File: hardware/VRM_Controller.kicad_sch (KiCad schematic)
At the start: 33 parts, among them J2001 Conn_01x02_Pin, J2002 Conn_01x02_Pin, J2003 Conn_01x02_Pin, J2004 Conn_01x02_Pin, U2001 TPS536C7B1RSLT

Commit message: feat(PCB): Vrms for mem and core layed out
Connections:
- net BVR_RDY is gone; now on net BRV_READY: R2014.2
- net at C2005.2, U2001.26 (AVSN): now also J2002.1 (Pin_1)
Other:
- note added: "Disconnecting the BVR_EN resistor will allow it to be configured by the micro controller as a Reset pin. The AVR_EN pin will controll both."
- note removed: "Add Reset Pin?"
- moved on the sheet: C2010, C2011, C2012, R2019, R2020

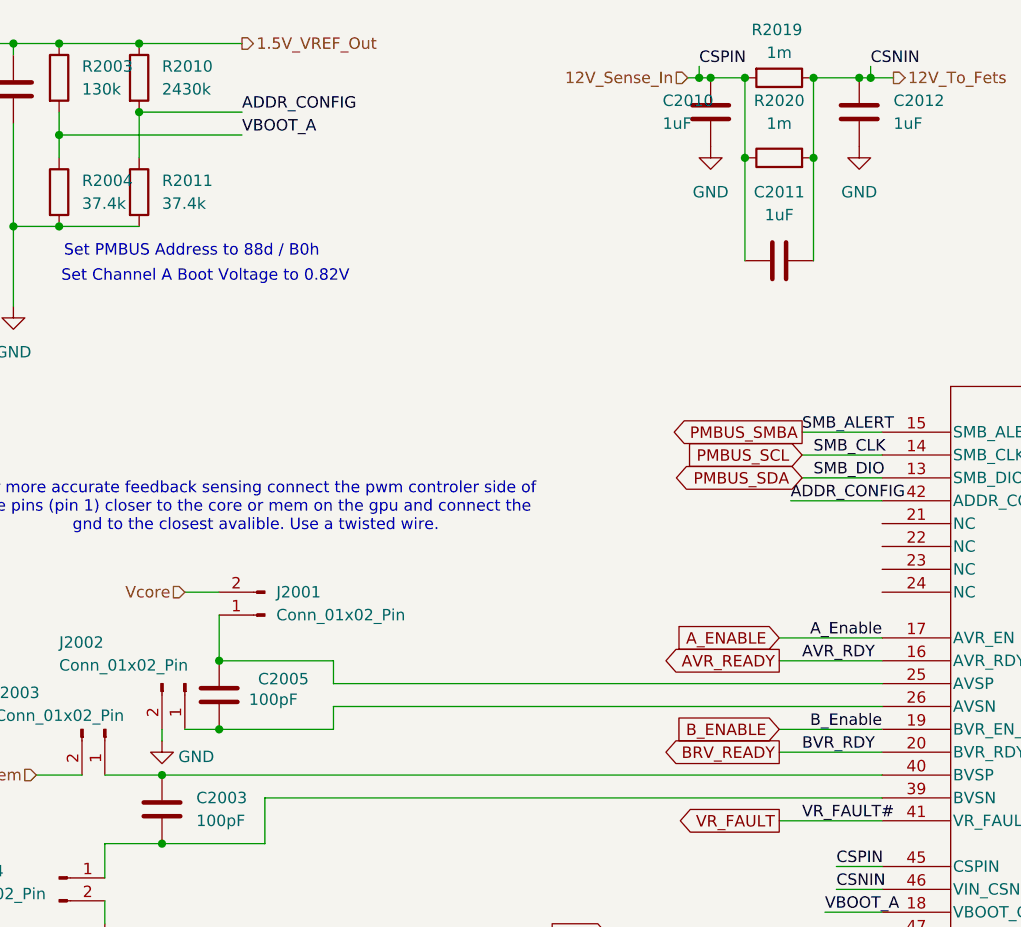
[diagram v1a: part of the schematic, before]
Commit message: feat(PCB): fix all DRC errors
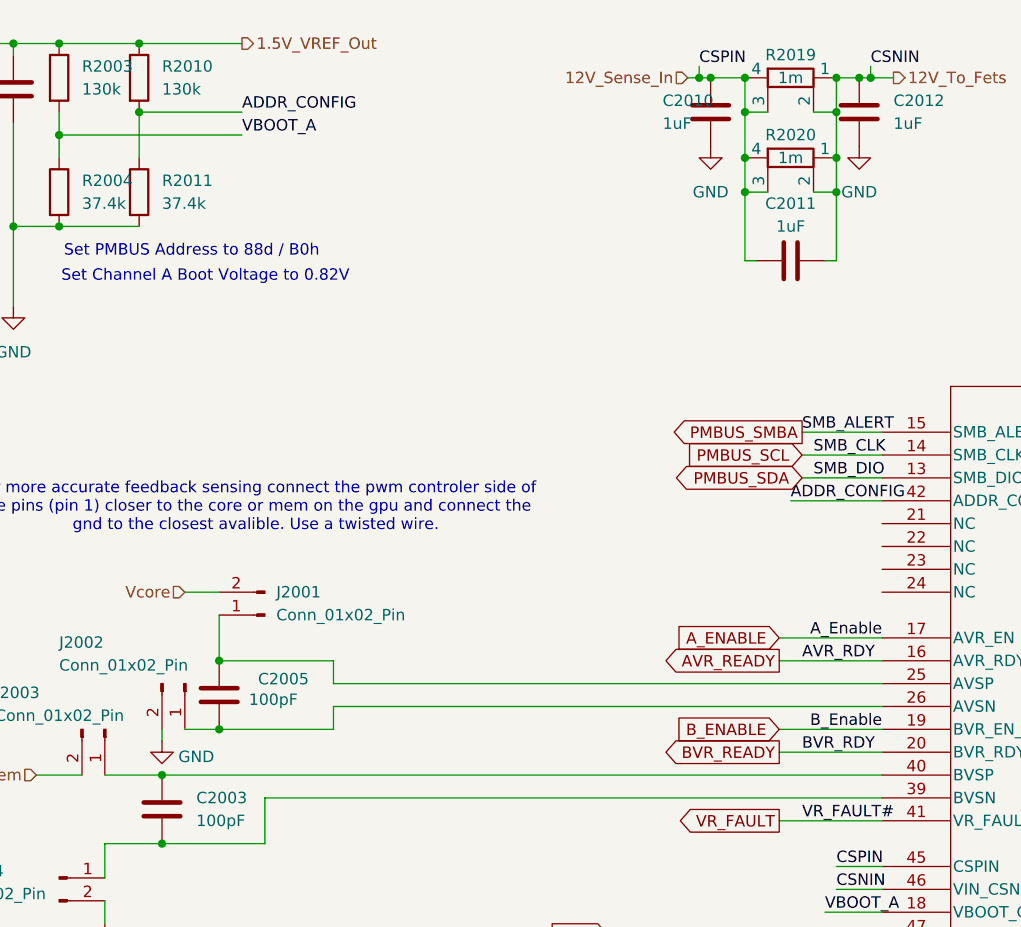
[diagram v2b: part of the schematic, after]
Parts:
- removed R2019: 1m, Resistor_SMD:R_Shunt_Vishay_WSK2512_6332Metric_T1.19mm, symbol Device:R
- added R2019: 1m, Resistor_SMD:R_Shunt_Vishay_WSK2512_6332Metric_T1.19mm, symbol Device:R_Shunt
- R2010: value 2430k -> 130k
- R2020: symbol Device:R -> Device:R_Shunt
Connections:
- net 12V_Sense_In: now also R2020.3, R2020.4, R2019.3, R2019.4; no longer R2020.1
- net 12V_To_Fets: now also R2020.1, R2019.1, R2019.2
- net BRV_READY renamed BVR_READY
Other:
- moved on the sheet: C2011

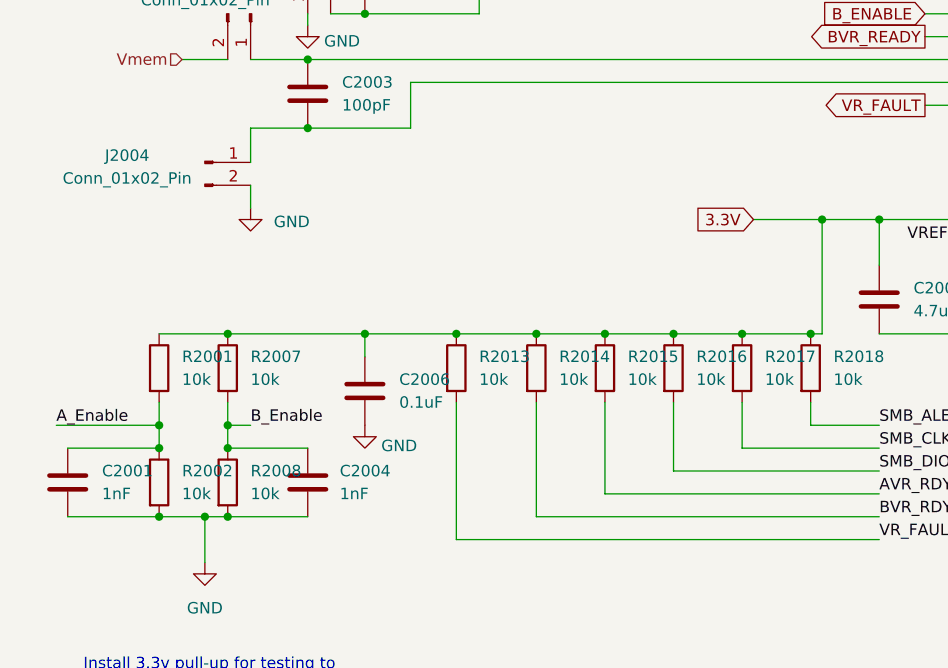
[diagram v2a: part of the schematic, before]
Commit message: feat(schematic): refactor main heirarchy
This commit makes a bunch of changes to how power is delivered on the
schematic. It also adds the probit header and the i2c output connector
on the main page of the schematic. Lastly, it changes it so that USB
power should work and also not power the 5V rail to the mosfet ICs.
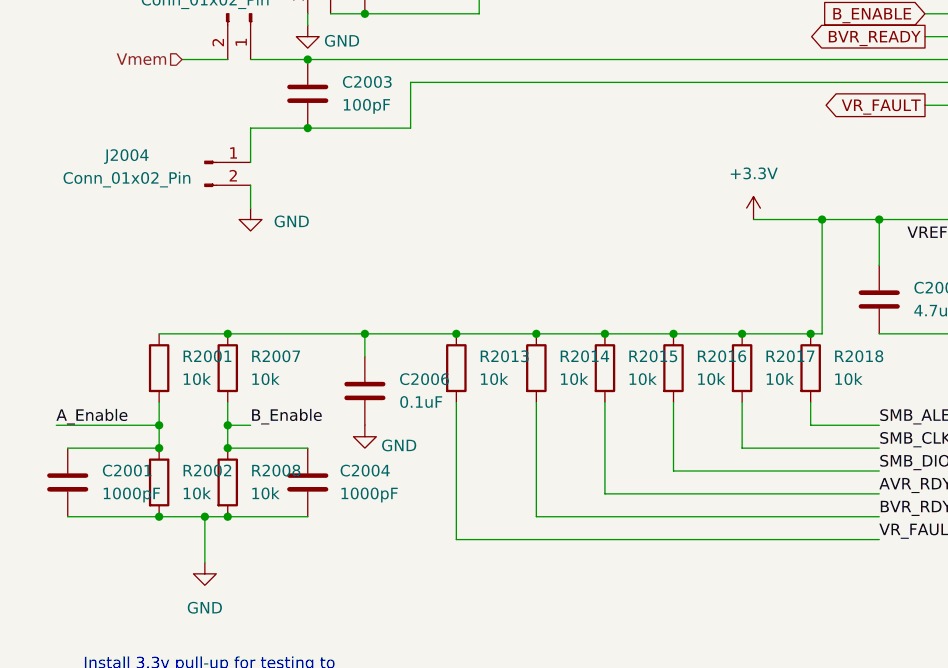
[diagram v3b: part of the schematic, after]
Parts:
- C2001, C2004: value 1nF -> 1000pF
- J2001, J2002, J2003, J2004: footprint Connector_PinHeader_2.54mm:PinHeader_1x02_P2.54mm_Vertical -> Connector_PinHeader_2.54mm:PinHeader_1x02_P2.54mm_Vertical_SMD_Pin1Right
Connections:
- net 3.3V renamed +3.3V
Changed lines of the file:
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@@
 	(label "CSPIN"
 		(at 101.6 20.32 0)
-		(fields_autoplaced yes)
 		(effects
 			(font
@@
 	(label "CSPIN"
 		(at 116.84 109.22 0)
-		(fields_autoplaced yes)
 		(effects
 			(font
@@
 	(label "VBOOT_A"
 		(at 115.57 114.3 0)
-		(fields_autoplaced yes)
 		(effects
 			(font
@@
 	(label "VR_FAULT#"
 		(at 113.03 104.14 0)
-		(fields_autoplaced yes)
 		(effects
 			(font
@@
 	(label "ADDR_CONFIG"
 		(at 111.76 68.58 0)
-		(fields_autoplaced yes)
 		(effects
 			(font
@@
 	(label "B_Enable"
 		(at 35.56 139.7 0)
-		(fields_autoplaced yes)
 		(effects
 			(font
@@
 	(label "VBOOT_A"
 		(at 50.8 27.94 0)
-		(fields_autoplaced yes)
 		(effects
 			(font
@@
 	(label "B_Enable"
 		(at 121.92 93.98 180)
-		(fields_autoplaced yes)
 		(effects
 			(font
@@
 	(label "AVR_RDY"
 		(at 113.03 86.36 0)
-		(fields_autoplaced yes)
 		(effects
 			(font
@@
 	(label "VREF"
 		(at 113.03 119.38 180)
-		(fields_autoplaced yes)
 		(effects
 			(font
@@
 	(label "CSNIN"
 		(at 120.65 20.32 0)
-		(fields_autoplaced yes)
 		(effects
 			(font
@@
 	(label "VREF"
 		(at 21.59 17.78 180)
-		(fields_autoplaced yes)
 		(effects
 			(font
@@
 	(label "CSNIN"
 		(at 116.84 111.76 0)
-		(fields_autoplaced yes)
 		(effects
 			(font
@@
 	(label "ADDR_CONFIG"
 		(at 50.8 25.4 0)
-		(fields_autoplaced yes)
 		(effects
 			(font
@@
 	(label "SMB_CLK"
 		(at 105.41 142.24 0)
-		(fields_autoplaced yes)
 		(effects
 			(font
@@
 	(label "SMB_ALERT"
 		(at 105.41 139.7 0)
-		(fields_autoplaced yes)
 		(effects
 			(font
@@
 	(label "SMB_CLK"
 		(at 114.3 63.5 0)
-		(fields_autoplaced yes)
 		(effects
 			(font
@@
 	(label "AVR_RDY"
 		(at 105.41 147.32 0)
-		(fields_autoplaced yes)
 		(effects
 			(font
@@
 	(label "BVR_RDY"
 		(at 113.03 96.52 0)
-		(fields_autoplaced yes)
 		(effects
 			(font
@@
 	(label "SMB_ALERT"
 		(at 113.03 60.96 0)
-		(fields_autoplaced yes)
 		(effects
 			(font
@@
 	(label "VR_FAULT#"
 		(at 105.41 152.4 0)
-		(fields_autoplaced yes)
 		(effects
 			(font
@@
 	(label "BVR_RDY"
 		(at 105.41 149.86 0)
-		(fields_autoplaced yes)
 		(effects
 			(font
@@
 	(label "A_Enable"
 		(at 121.92 83.82 180)
-		(fields_autoplaced yes)
 		(effects
 			(font
@@
 	(label "SMB_DIO"
 		(at 114.3 66.04 0)
-		(fields_autoplaced yes)
 		(effects
 			(font
@@
 	(label "SMB_DIO"
 		(at 105.41 144.78 0)
-		(fields_autoplaced yes)
 		(effects
 			(font
@@
 	(label "A_Enable"
 		(at 13.97 139.7 0)
-		(fields_autoplaced yes)
 		(effects
 			(font
@@
 		)
 	)
-	(global_label "3.3V"
-		(shape input)
-		(at 91.44 116.84 180)
-		(fields_autoplaced yes)
-		(effects
-			(font
-				(size 1.27 1.27)
-			)
-			(justify right)
-		)
-		(property "Intersheetrefs" "${INTERSHEET_REFS}"
-			(at 84.3424 116.84 0)
-			(effects
-				(font
-					(size 1.27 1.27)
-				)
-				(justify right)
-				(hide yes)
-			)
-		)
-	)
 	(hierarchical_label "Vmem"
 		(shape input)
 		(at 27.94 99.06 180)
-		(fields_autoplaced yes)
 		(effects
 			(font
@@
 		(shape input)
 		(at 100.33 21.59 180)
-		(fields_autoplaced yes)
 		(effects
 			(font
@@
 		(shape input)
 		(at 177.8 86.36 0)
-		(fields_autoplaced yes)
 		(effects
 			(font
@@
 		(shape input)
 		(at 177.8 81.28 0)
-		(fields_autoplaced yes)
 		(effects
 			(font
@@
 		(shape input)
 		(at 179.07 129.54 0)
-		(fields_autoplaced yes)
 		(effects
 			(font
@@
 		(shape output)
 		(at 177.8 68.58 0)
-		(fields_autoplaced yes)
 		(effects
 			(font
@@
 		(shape input)
 		(at 177.8 119.38 0)
-		(fields_autoplaced yes)
 		(effects
 			(font
@@
 		(shape input)
 		(at 177.8 91.44 0)
-		(fields_autoplaced yes)
 		(effects
 			(font
@@
 		(shape input)
 		(at 177.8 114.3 0)
-		(fields_autoplaced yes)
 		(effects
 			(font
@@
 		(shape output)
 		(at 177.8 99.06 0)
-		(fields_autoplaced yes)
 		(effects
 			(font
@@
 		(shape input)
 		(at 177.8 101.6 0)
-		(fields_autoplaced yes)
 		(effects
 			(font
@@
 		(shape output)
 		(at 177.8 93.98 0)
-		(fields_autoplaced yes)
 		(effects
 			(font
@@
 		(shape output)
 		(at 123.19 21.59 0)
-		(fields_autoplaced yes)
 		(effects
 			(font
@@
 		(shape output)
 		(at 177.8 104.14 0)
-		(fields_autoplaced yes)
 		(effects
 			(font
@@
 		(shape input)
 		(at 196.85 127 0)
-		(fields_autoplaced yes)
 		(effects
 			(font
@@
 		(shape input)
 		(at 177.8 106.68 0)
-		(fields_autoplaced yes)
 		(effects
 			(font
@@
 		(shape input)
 		(at 177.8 66.04 0)
-		(fields_autoplaced yes)
 		(effects
 			(font
@@
 		(shape input)
 		(at 177.8 76.2 0)
-		(fields_autoplaced yes)
 		(effects
 			(font
@@
 		(shape input)
 		(at 44.45 78.74 180)
-		(fields_autoplaced yes)
 		(effects
 			(font
@@
 		(shape input)
 		(at 177.8 71.12 0)
-		(fields_autoplaced yes)
 		(effects
 			(font
@@
 		(shape output)
 		(at 177.8 83.82 0)
-		(fields_autoplaced yes)
 		(effects
 			(font
@@
 		(shape output)
 		(at 177.8 63.5 0)
-		(fields_autoplaced yes)
 		(effects
 			(font
@@
 		(shape input)
 		(at 177.8 60.96 0)
-		(fields_autoplaced yes)
 		(effects
 			(font
@@
 		(shape output)
 		(at 177.8 73.66 0)
-		(fields_autoplaced yes)
 		(effects
 			(font
@@
 		(shape output)
 		(at 177.8 88.9 0)
-		(fields_autoplaced yes)
 		(effects
 			(font
@@
 		(shape output)
 		(at 50.8 17.78 0)
-		(fields_autoplaced yes)
 		(effects
 			(font
@@
 		(shape output)
 		(at 177.8 121.92 0)
-		(fields_autoplaced yes)
 		(effects
 			(font
@@
 		(shape input)
 		(at 177.8 96.52 0)
-		(fields_autoplaced yes)
 		(effects
 			(font
@@
 		(shape output)
 		(at 177.8 78.74 0)
-		(fields_autoplaced yes)
 		(effects
 			(font
@@
 		(shape output)
 		(at 177.8 116.84 0)
-		(fields_autoplaced yes)
 		(effects
 			(font
@@
 		(shape output)
 		(at 177.8 109.22 0)
-		(fields_autoplaced yes)
 		(effects
 			(font
@@
 			)
 		)
-		(property "Value" "1nF"
+		(property "Value" "1000pF"
 			(at 19.05 147.3199 0)
 			(effects
@@
 	)
 	(symbol
+		(lib_id "power:+3.3V")
+		(at 91.44 116.84 0)
+		(unit 1)
+		(exclude_from_sim no)
+		(in_bom yes)
+		(on_board yes)
+		(dnp no)
+		(fields_autoplaced yes)
+		(property "Reference" "#PWR02010"
+			(at 91.44 120.65 0)
+			(effects
+				(font
+					(size 1.27 1.27)
+				)
+				(hide yes)
+			)
+		)
+		(property "Value" "+3.3V"
+			(at 91.44 111.76 0)
+			(effects
+				(font
+					(size 1.27 1.27)
+				)
+			)
+		)
+		(property "Footprint" ""
+			(at 91.44 116.84 0)
+			(effects
+				(font
+					(size 1.27 1.27)
+				)
+				(hide yes)
+			)
+		)
+		(property "Datasheet" ""
+			(at 91.44 116.84 0)
+			(effects
+				(font
+					(size 1.27 1.27)
+				)
+				(hide yes)
+			)
+		)
+		(property "Description" "Power symbol creates a global label with name \"+3.3V\""
+			(at 91.44 116.84 0)
+			(effects
+				(font
+					(size 1.27 1.27)
+				)
+				(hide yes)
+			)
+		)
+		(pin "1"
+		)
+		(instances
+			(project ""
+				(path "/d5303413-7068-41ba-88e3-39dfa38d31b7/e6dc7bfe-1f99-4466-9581-badeb70bd091"
+					(reference "#PWR02010")
+					(unit 1)
+				)
+			)
+		)
+	)
+	(symbol
 		(lib_id "Device:C")
 		(at 105.41 125.73 0)
@@
 			)
 		)
-		(property "Footprint" "Connector_PinHeader_2.54mm:PinHeader_1x02_P2.54mm_Vertical"
+		(property "Footprint" "Connector_PinHeader_2.54mm:PinHeader_1x02_P2.54mm_Vertical_SMD_Pin1Right"
 			(at 53.34 81.28 0)
 			(effects
@@
 			)
 		)
-		(property "Footprint" "Connector_PinHeader_2.54mm:PinHeader_1x02_P2.54mm_Vertical"
+		(property "Footprint" "Connector_PinHeader_2.54mm:PinHeader_1x02_P2.54mm_Vertical_SMD_Pin1Right"
 			(at 44.45 88.9 0)
 			(effects
@@
 			)
 		)
-		(property "Footprint" "Connector_PinHeader_2.54mm:PinHeader_1x02_P2.54mm_Vertical"
+		(property "Footprint" "Connector_PinHeader_2.54mm:PinHeader_1x02_P2.54mm_Vertical_SMD_Pin1Right"
 			(at 35.56 93.98 0)
 			(effects
@@
 			)
 		)
-		(property "Footprint" "Connector_PinHeader_2.54mm:PinHeader_1x02_P2.54mm_Vertical"
+		(property "Footprint" "Connector_PinHeader_2.54mm:PinHeader_1x02_P2.54mm_Vertical_SMD_Pin1Right"
 			(at 30.48 110.49 0)
 			(effects
@@
 			)
 		)
-		(property "Value" "1nF"
+		(property "Value" "1000pF"
 			(at 45.466 147.32 0)
 			(effects

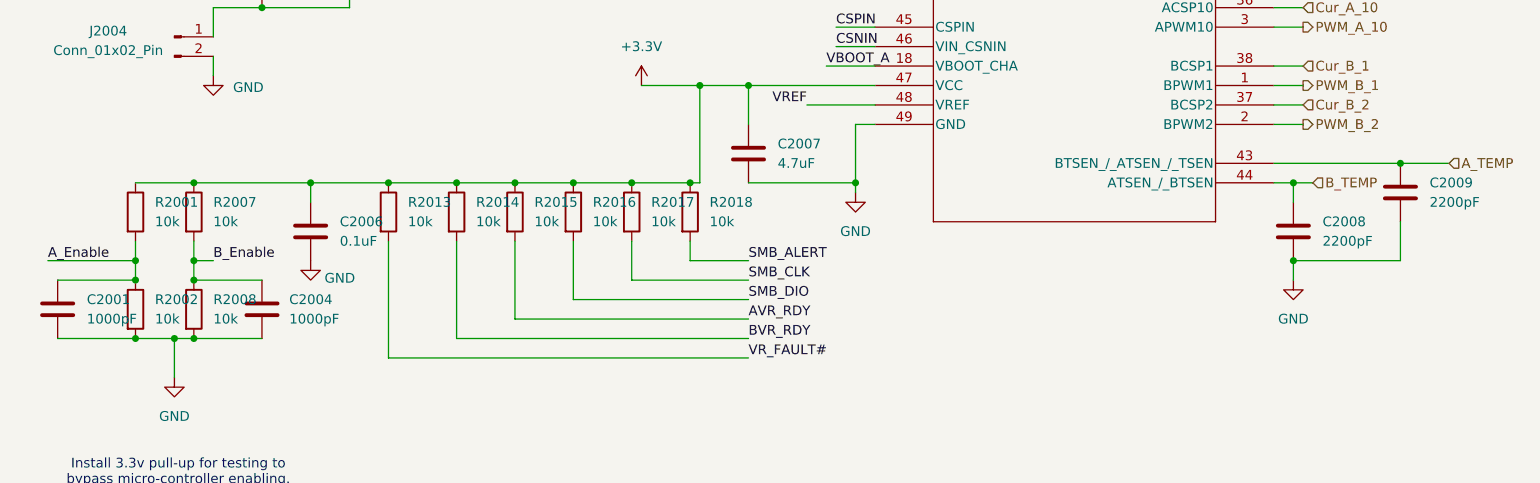
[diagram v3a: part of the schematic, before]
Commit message: feat(schematic): added cooler mounting holes
added cooler mounting holes to schematic
changed temp pins to read proper tempurature
small fixes
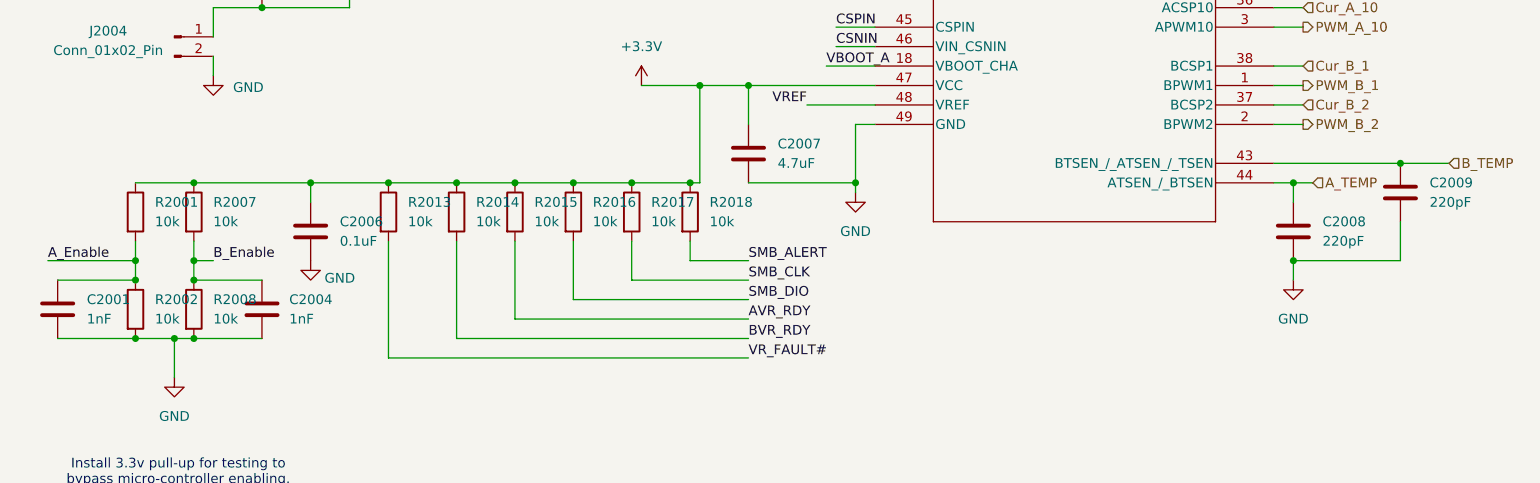
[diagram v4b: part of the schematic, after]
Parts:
- C2001, C2004: value 1000pF -> 1nF; footprint Capacitor_SMD:C_0805_2012Metric -> Capacitor_SMD:C_0402_1005Metric
- C2002, C2003, C2005, C2006, C2007, C2010, C2011, C2012: footprint Capacitor_SMD:C_0805_2012Metric -> Capacitor_SMD:C_0402_1005Metric
- C2008, C2009: value 2200pF -> 220pF; footprint Capacitor_SMD:C_0805_2012Metric -> Capacitor_SMD:C_0402_1005Metric
- J2001, J2002, J2003, J2004: footprint Connector_PinHeader_2.54mm:PinHeader_1x02_P2.54mm_Vertical_SMD_Pin1Right -> Connector_PinHeader_2.54mm:PinHeader_1x02_P2.54mm_Vertical_SMD_Pin1Left
- R2003, R2010: footprint Resistor_SMD:R_0805_2012Metric -> Resistor_SMD:R_0603_1608Metric
- R2004, R2011: footprint Resistor_SMD:R_0805_2012Metric -> Resistor_SMD:R_0402_1005Metric
- R2013, R2014, R2015, R2016, R2017, R2018: footprint Resistor_SMD:R_0805_2012Metric -> Resistor_SMD:R_0201_0603Metric
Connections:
- net A_TEMP: now also C2008.1, U2001.44 (ATSEN_/_BTSEN); no longer C2009.1, U2001.43 (BTSEN_/_ATSEN_/_TSEN)
- net B_TEMP: now also C2009.1, U2001.43 (BTSEN_/_ATSEN_/_TSEN); no longer C2008.1, U2001.44 (ATSEN_/_BTSEN)
